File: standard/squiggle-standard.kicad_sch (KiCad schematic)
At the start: 36 parts

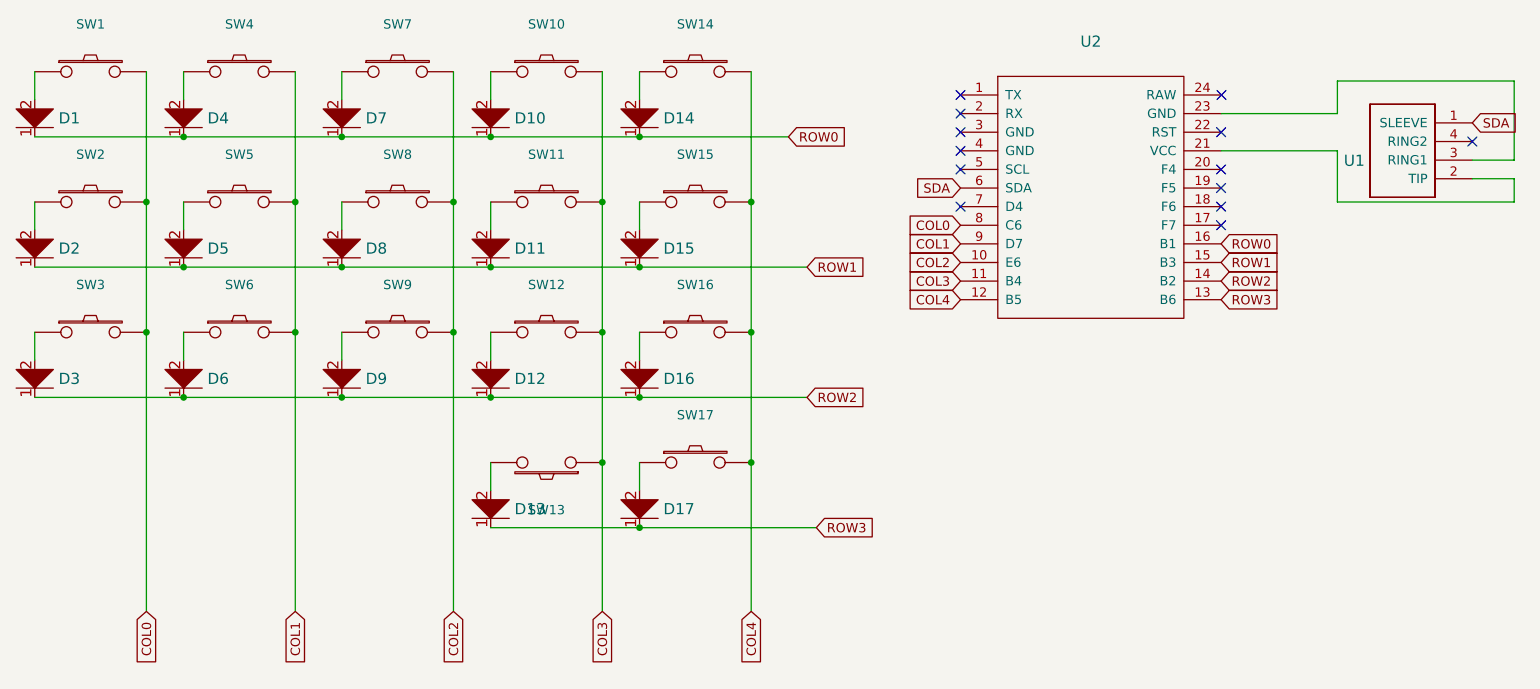
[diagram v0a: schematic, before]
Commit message: added encoder to schematic and wired switch pinouts
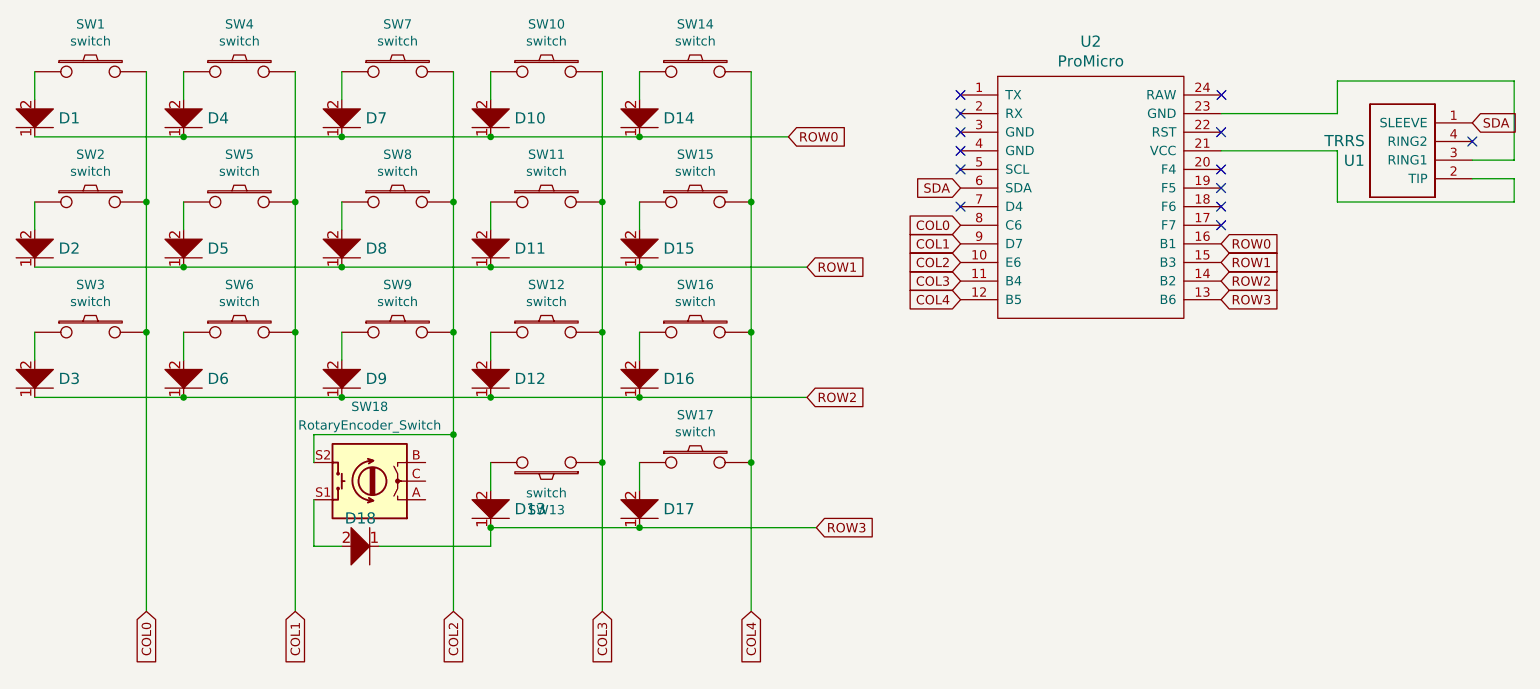
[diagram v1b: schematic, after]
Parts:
- added D18: diode, symbol squiggle:diode
- added SW18: RotaryEncoder_Switch, symbol Device:RotaryEncoder_Switch
- D1, D10, D11, D12, D13, D14, D15, D16, D17, D2, D3, D4, D5, D6, D7, D8, D9: value (none) -> D; footprint (none) -> footprints:diode
- SW1, SW10, SW11, SW12, SW14, SW15, SW16, SW2, SW3, SW4, SW5, SW6, SW7, SW8, SW9: value (none) -> switch; footprint (none) -> footprints:1u-dual
- SW13, SW17: value (none) -> switch; footprint (none) -> footprints:2u-dual
- U1: value (none) -> TRRS; footprint (none) -> footprints:trrs
- U2: value (none) -> ProMicro; footprint (none) -> footprints:promicro
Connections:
- net COL2: now also SW18.S2
- net ROW3: now also D18.1
- new net: D18.2, SW18.S1
